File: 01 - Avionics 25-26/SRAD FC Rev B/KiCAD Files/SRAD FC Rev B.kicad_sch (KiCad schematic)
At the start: 0 parts

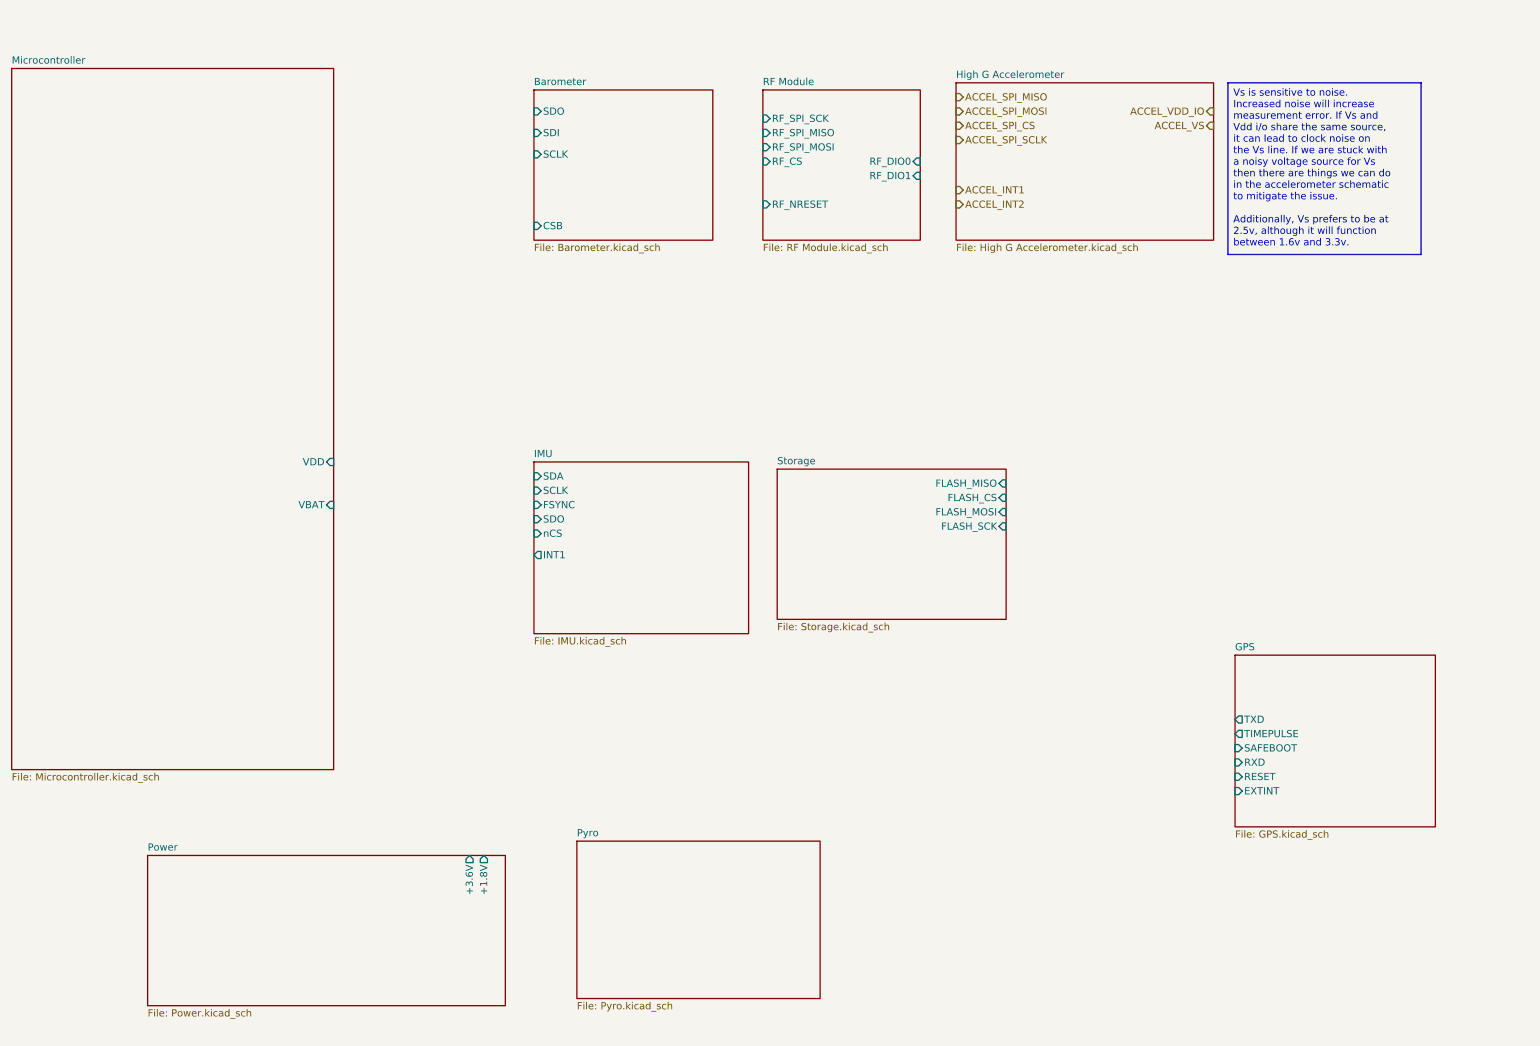
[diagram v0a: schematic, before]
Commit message: added some pins for the MCU related to debugger, also added reset button for MCU
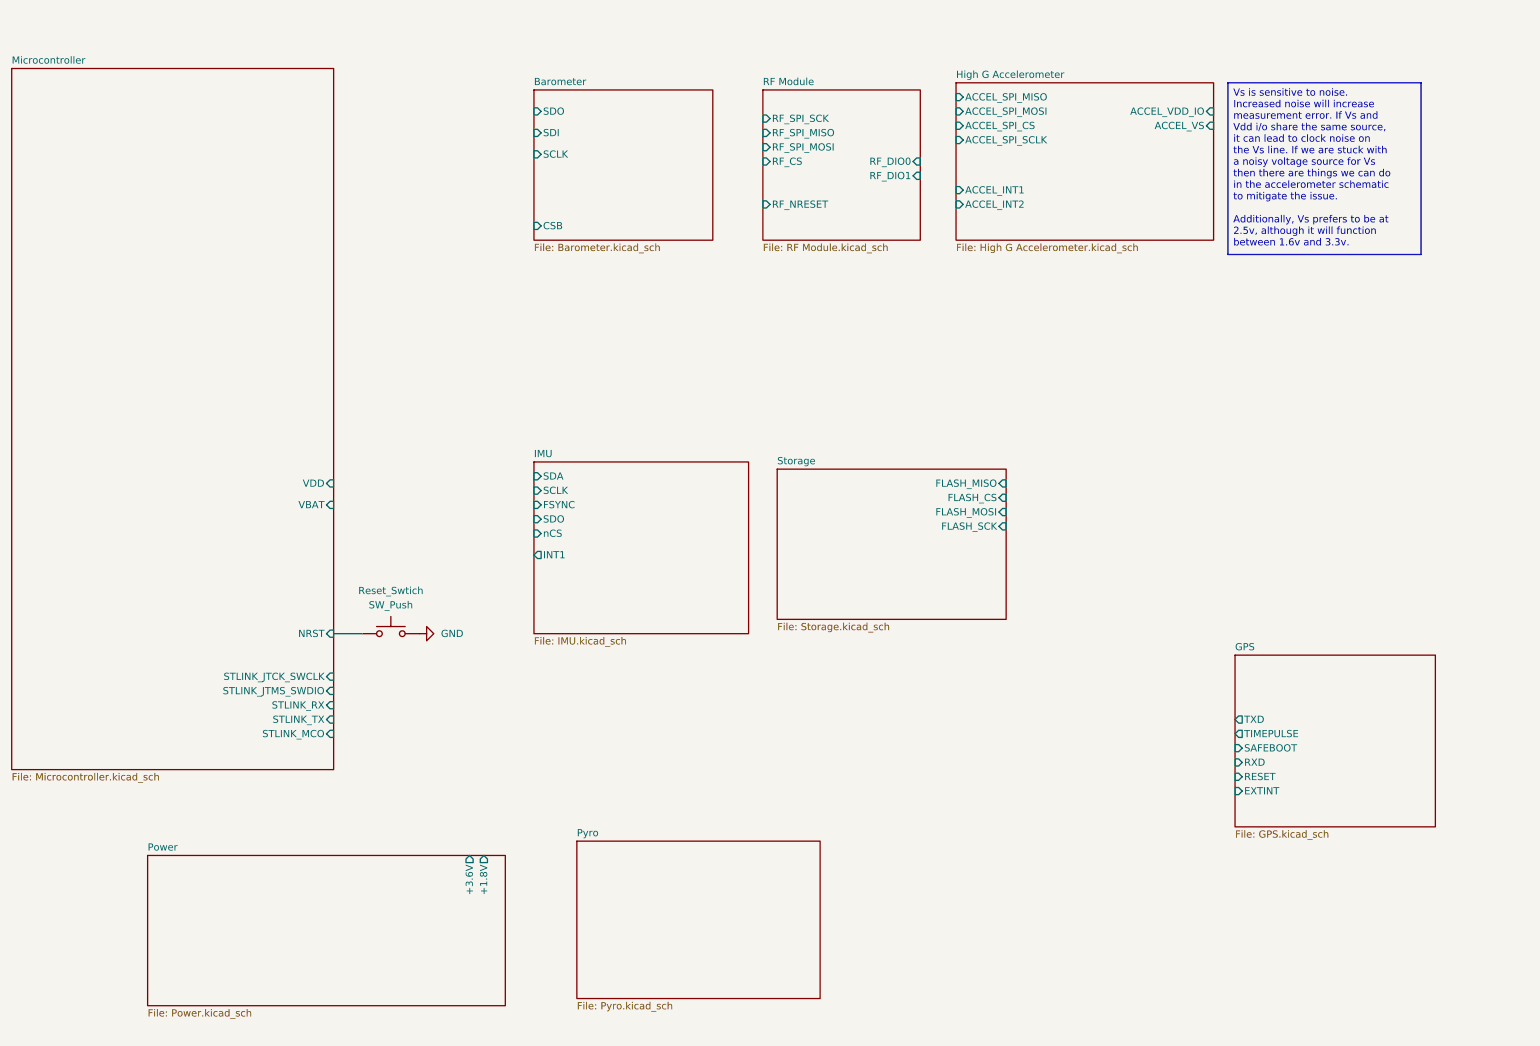
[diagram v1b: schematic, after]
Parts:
- added Reset_Swtich: SW_Push, symbol Switch:SW_Push
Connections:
- new net GND: Reset_Swtich.2
- new net Microcontroller/NRST: Reset_Swtich.1
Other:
- sheet High G Accelerometer ports: added ACCEL_INT1, ACCEL_INT2, ACCEL_SPI_CS, ACCEL_SPI_MISO, ACCEL_SPI_MOSI, ACCEL_SPI_SCLK, ACCEL_VDD_IO, ACCEL_VS; removed none
- sheet Microcontroller ports: added NRST, STLINK_JTCK_SWCLK, STLINK_JTMS_SWDIO, STLINK_MCO, STLINK_RX, STLINK_TX; removed none

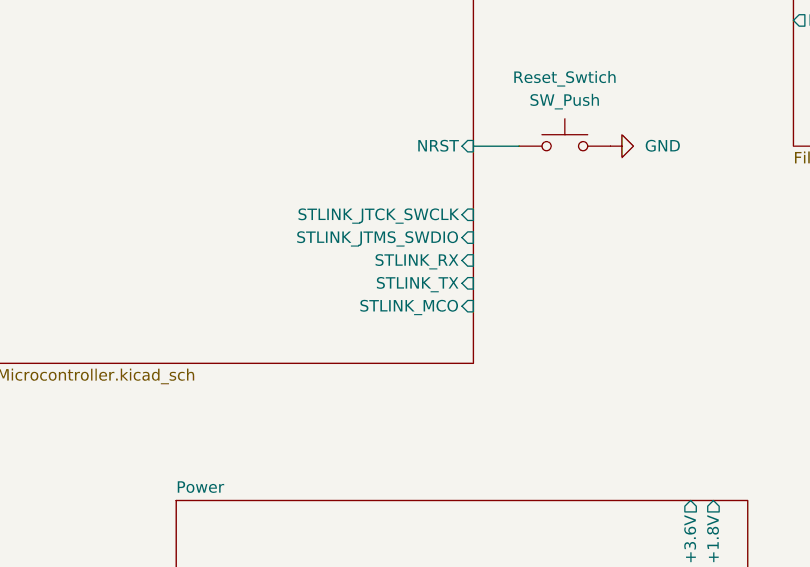
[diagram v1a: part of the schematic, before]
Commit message: removed unneccessary debug wires
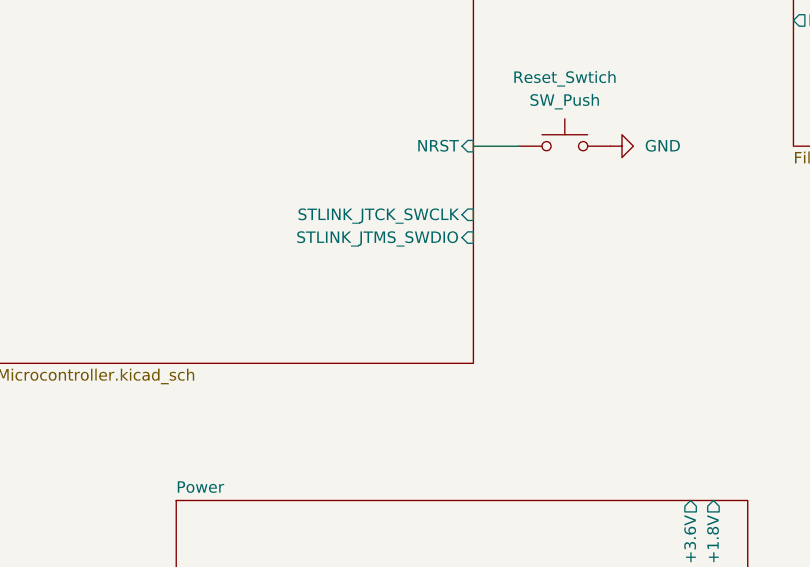
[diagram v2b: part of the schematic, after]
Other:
- sheet Microcontroller ports: added none; removed STLINK_MCO, STLINK_RX, STLINK_TX
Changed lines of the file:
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@@
-			)
-		)
-		(pin "STLINK_TX" input
-			(at 78.74 138.43 0)
-			(effects
-				(font
-					(size 1.27 1.27)
-				)
-				(justify right)
-			)
-		)
-		(pin "STLINK_MCO" input
-			(at 78.74 140.97 0)
-			(effects
-				(font
-					(size 1.27 1.27)
-				)
-				(justify right)
-			)
-		)
-		(pin "STLINK_RX" input
-			(at 78.74 135.89 0)
-			(effects
-				(font
-					(size 1.27 1.27)
-				)
-				(justify right)
 			)
 		)

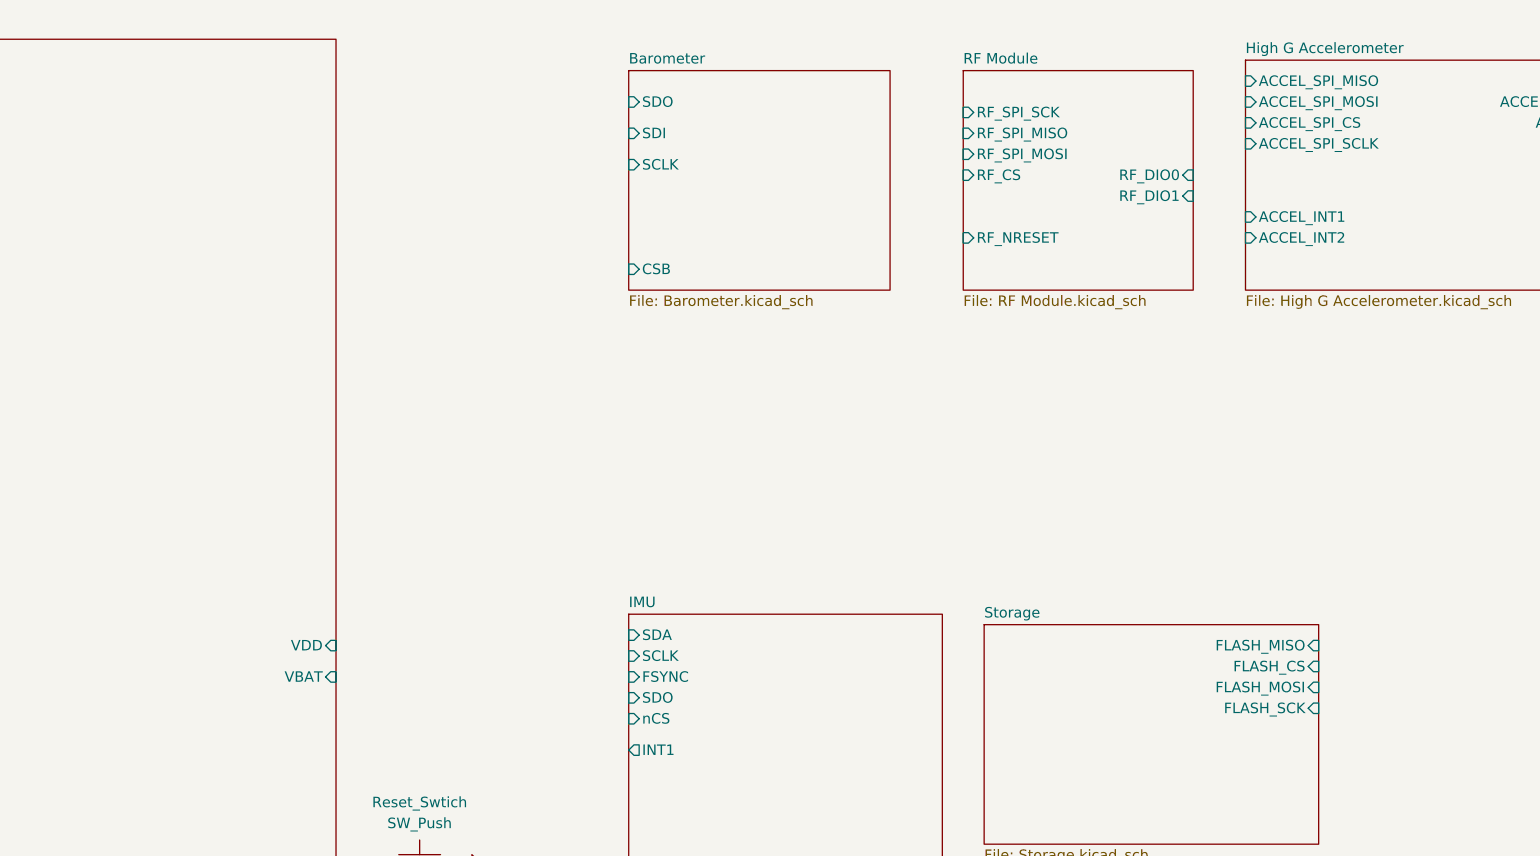
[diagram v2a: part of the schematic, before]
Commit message: wired spi bus in top level sheet
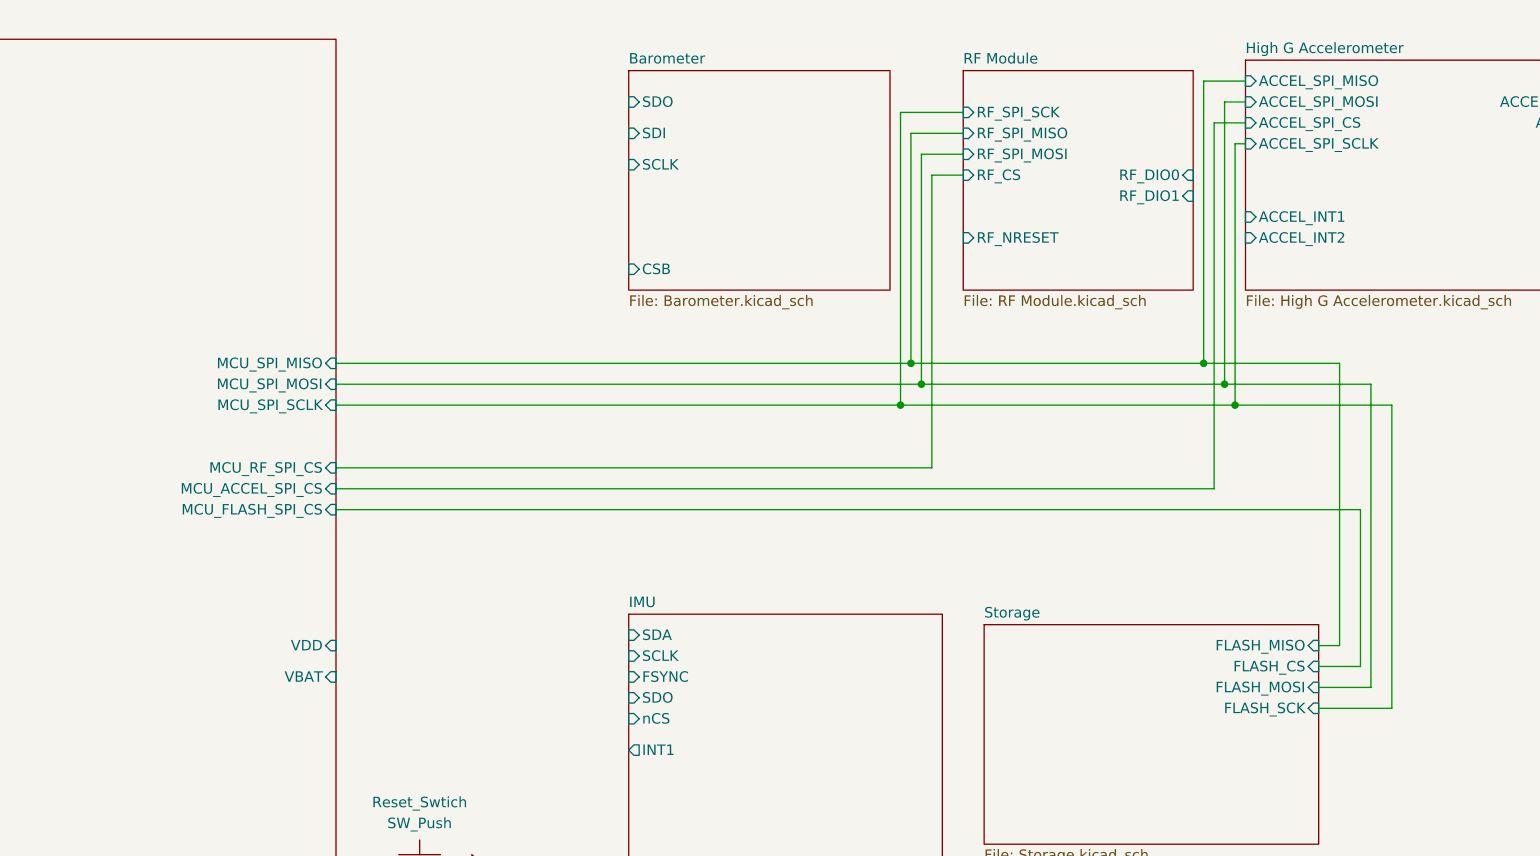
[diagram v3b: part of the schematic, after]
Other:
- sheet Microcontroller ports: added MCU_ACCEL_SPI_CS, MCU_FLASH_SPI_CS, MCU_RF_SPI_CS, MCU_SPI_MISO, MCU_SPI_MOSI, MCU_SPI_SCLK; removed none

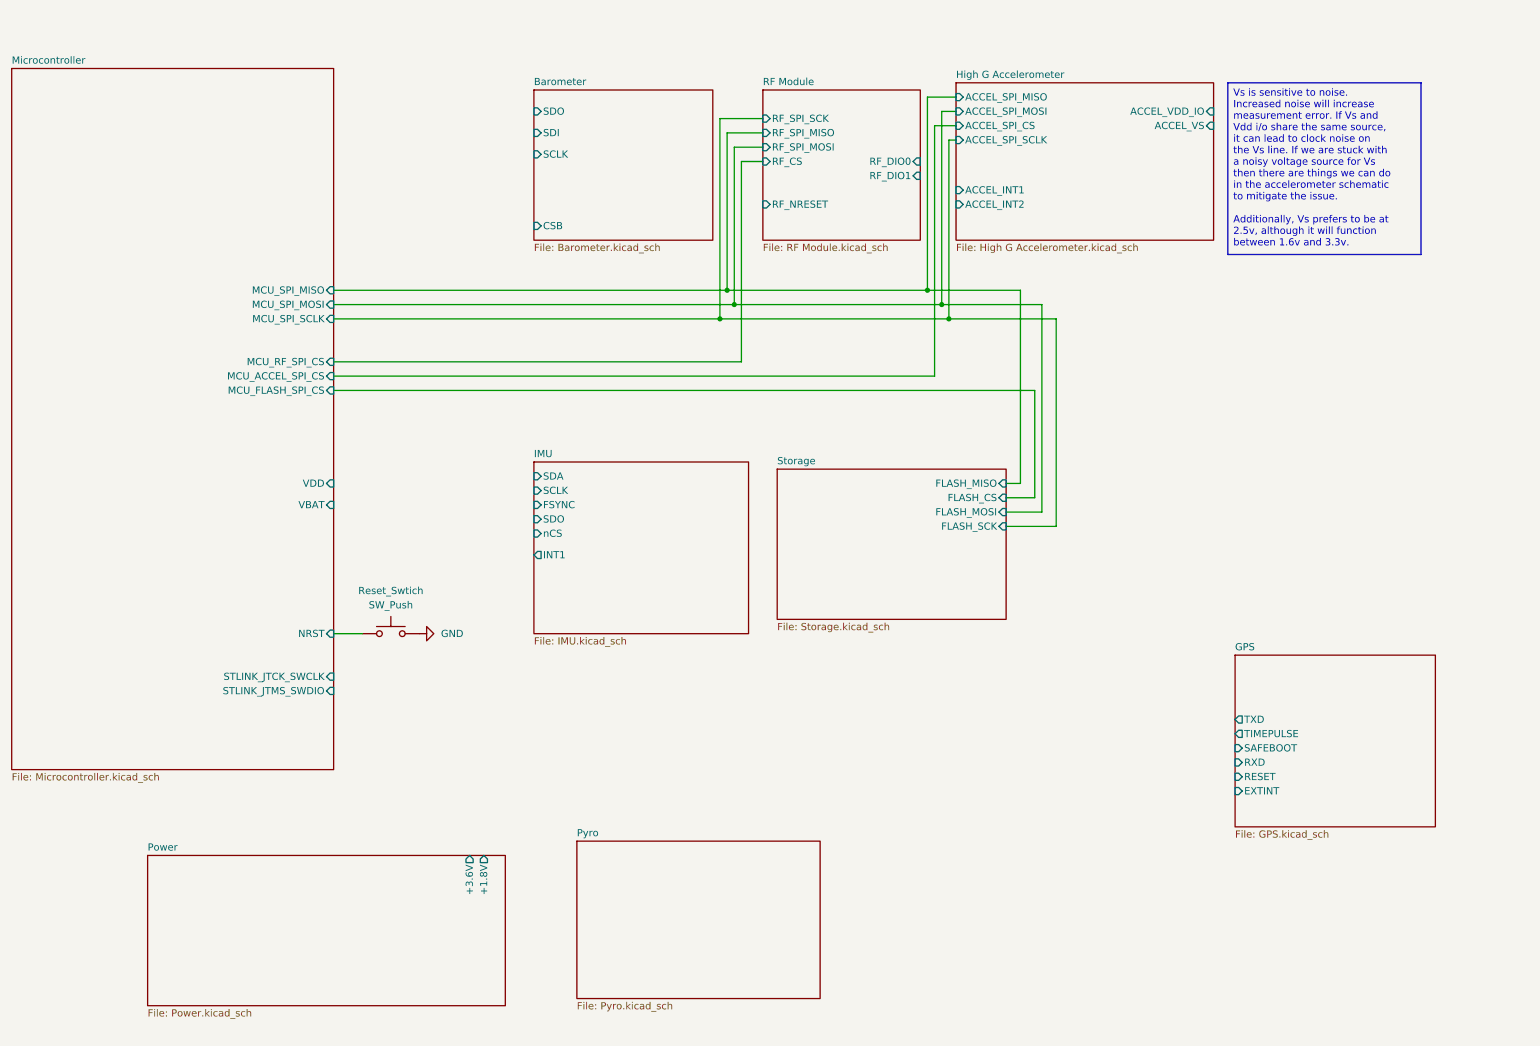
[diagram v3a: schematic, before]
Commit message: moved stuff arround, added connector for debugging
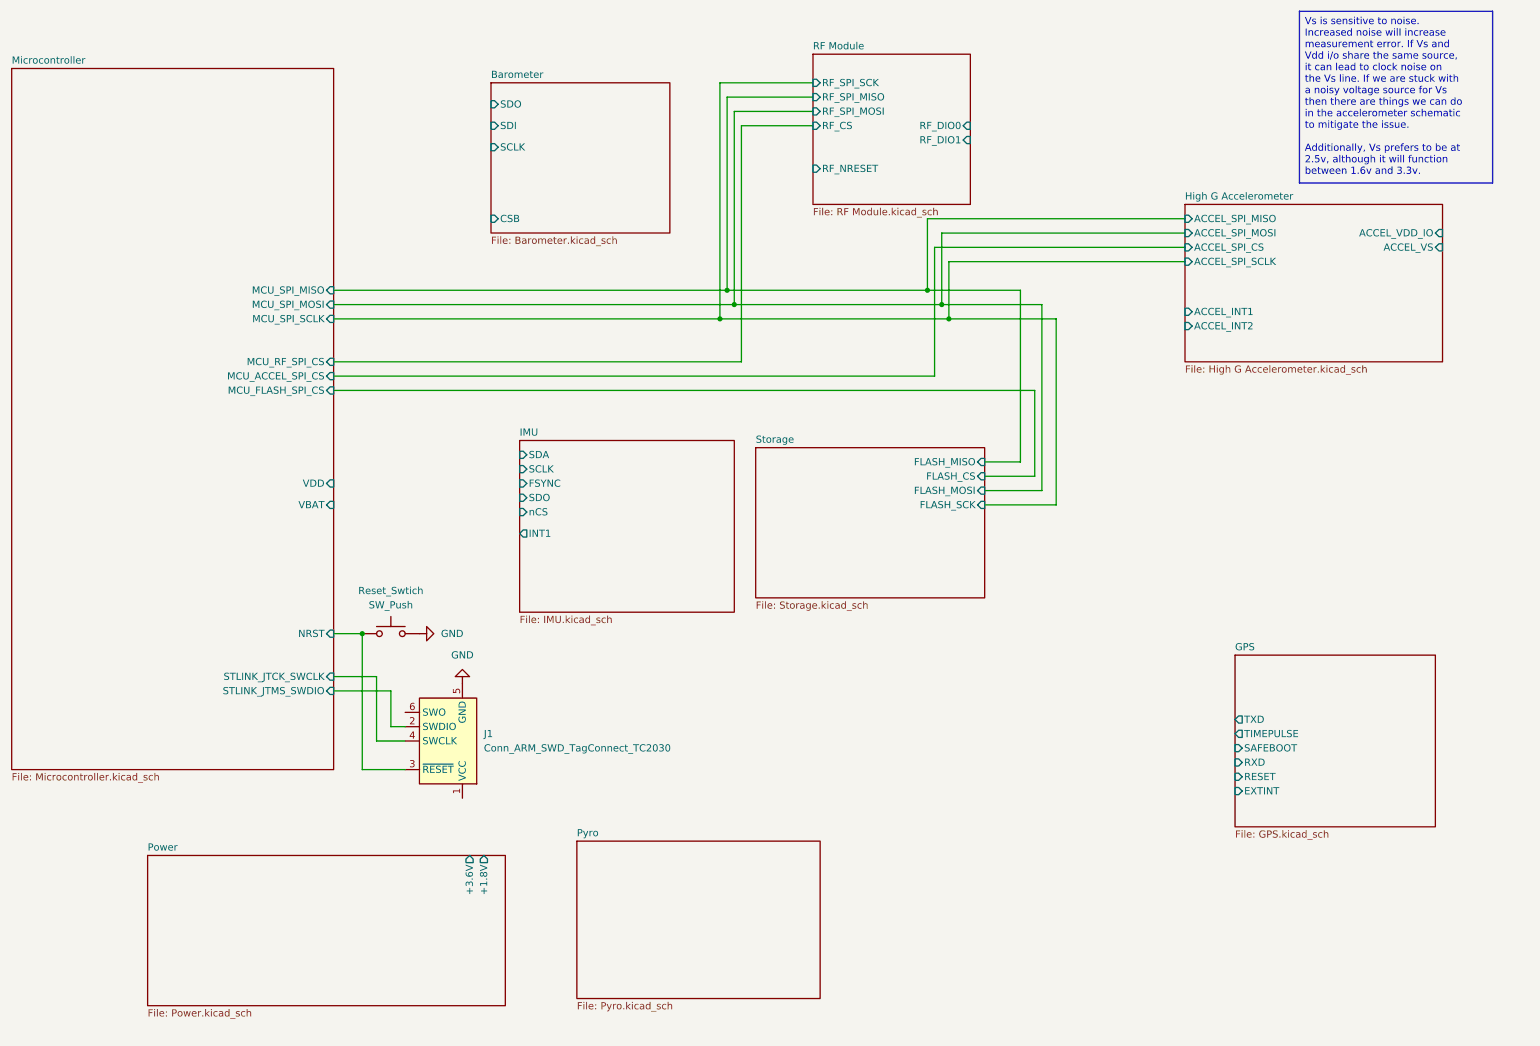
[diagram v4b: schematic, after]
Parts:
- added J1: Conn_ARM_SWD_TagConnect_TC2030, Connector:Tag-Connect_TC2030-IDC-FP_2x03_P1.27mm_Vertical, symbol Connector:Conn_ARM_SWD_TagConnect_TC2030
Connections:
- net GND: now also J1.5 (GND)
- net Microcontroller/NRST: now also J1.3 (~{RESET})
- net Microcontroller/STLINK_JTCK_SWCLK: now also J1.4 (SWCLK)
- net Microcontroller/STLINK_JTMS_SWDIO: now also J1.2 (SWDIO)

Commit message: continued wiring spi bus
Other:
- sheet Microcontroller ports: added MCU_BARO_SPI_CS, MCU_IMU_SPI_CS; removed none
